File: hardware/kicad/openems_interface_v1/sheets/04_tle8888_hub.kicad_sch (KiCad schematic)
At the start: 5 parts, among them U3 TLE8888-2QK

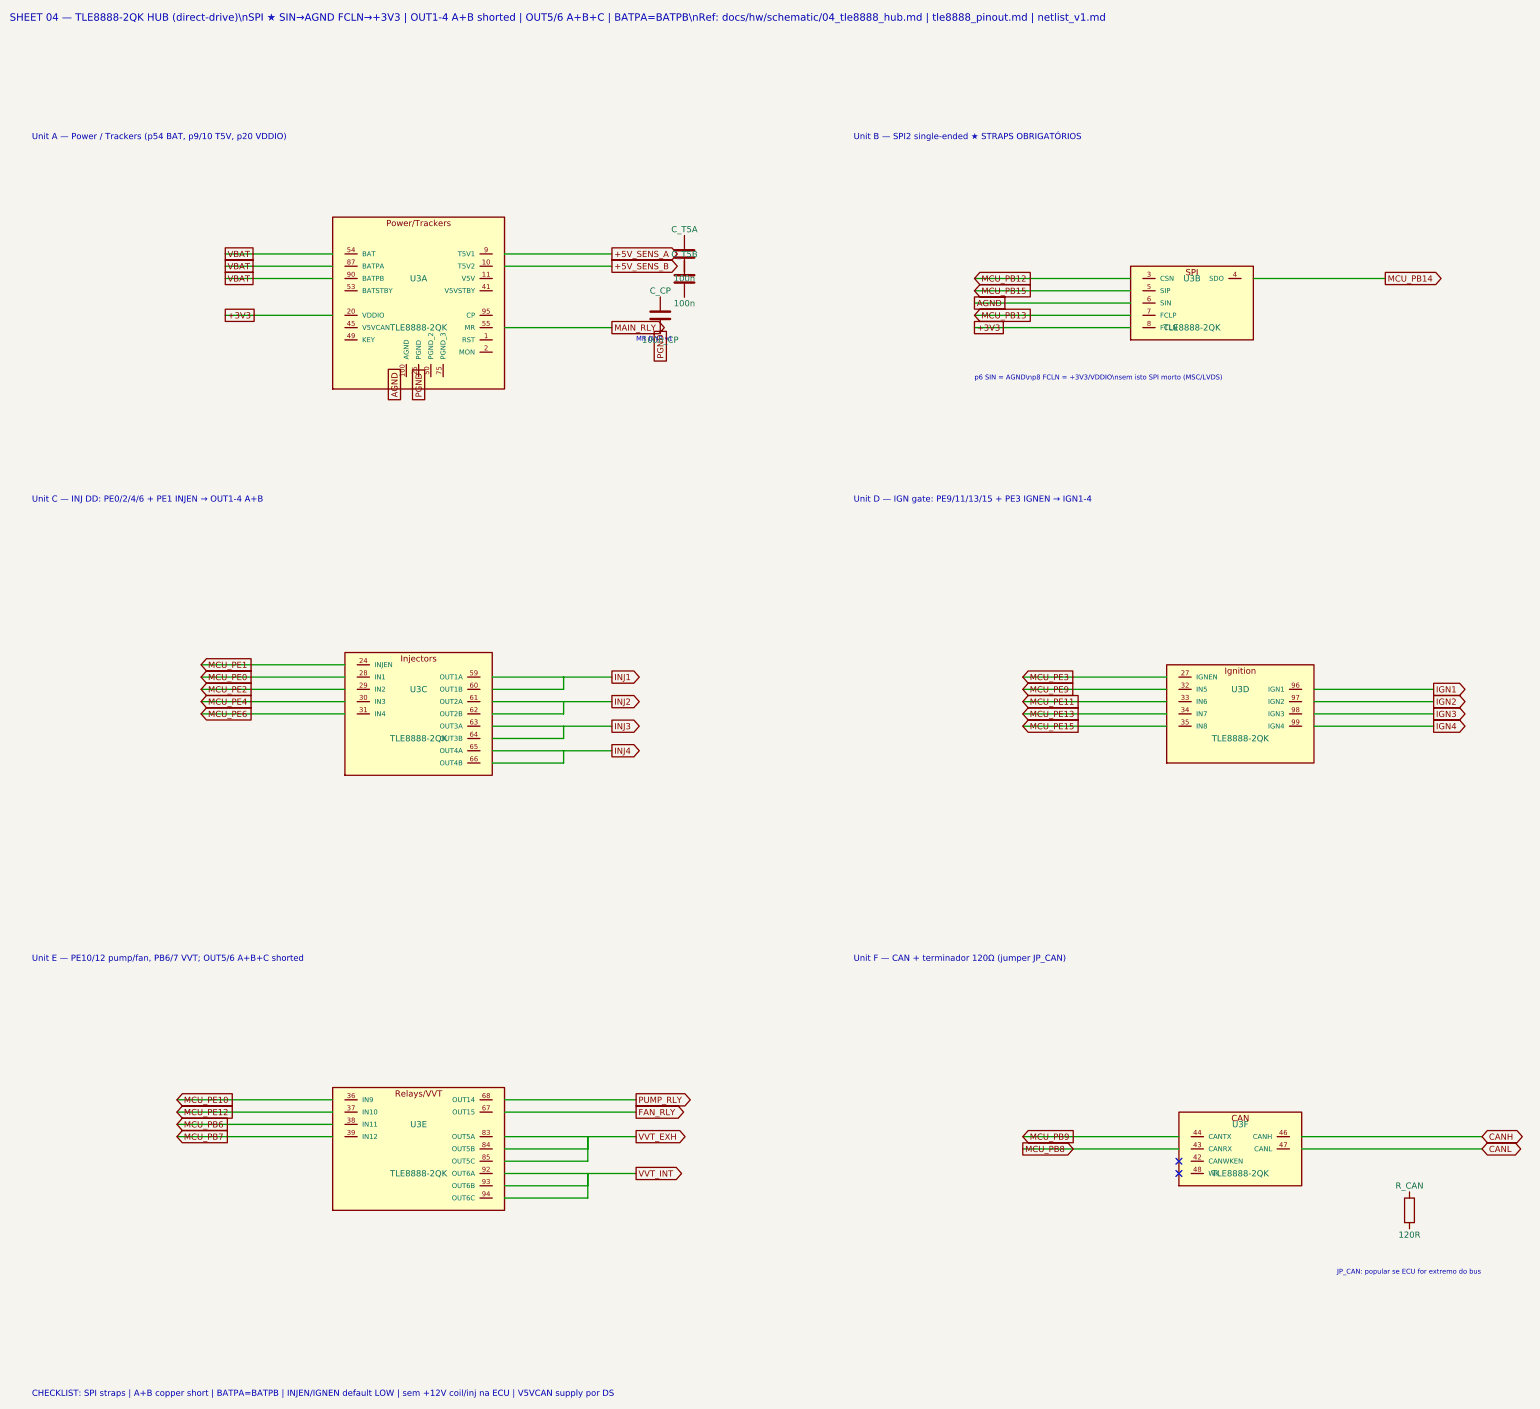
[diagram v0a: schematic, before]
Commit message: feat(hw): nets J1/J2 no PCB + zones PGND + star GND no sch
Atribui pads AMPSEAL a partir de pinmap_logical.md (autoridade),
adiciona pours PGND F/B, e evita curto de terras no esquemático
(star só via NetTie no layout). Script annotate_pcb_nets.py.
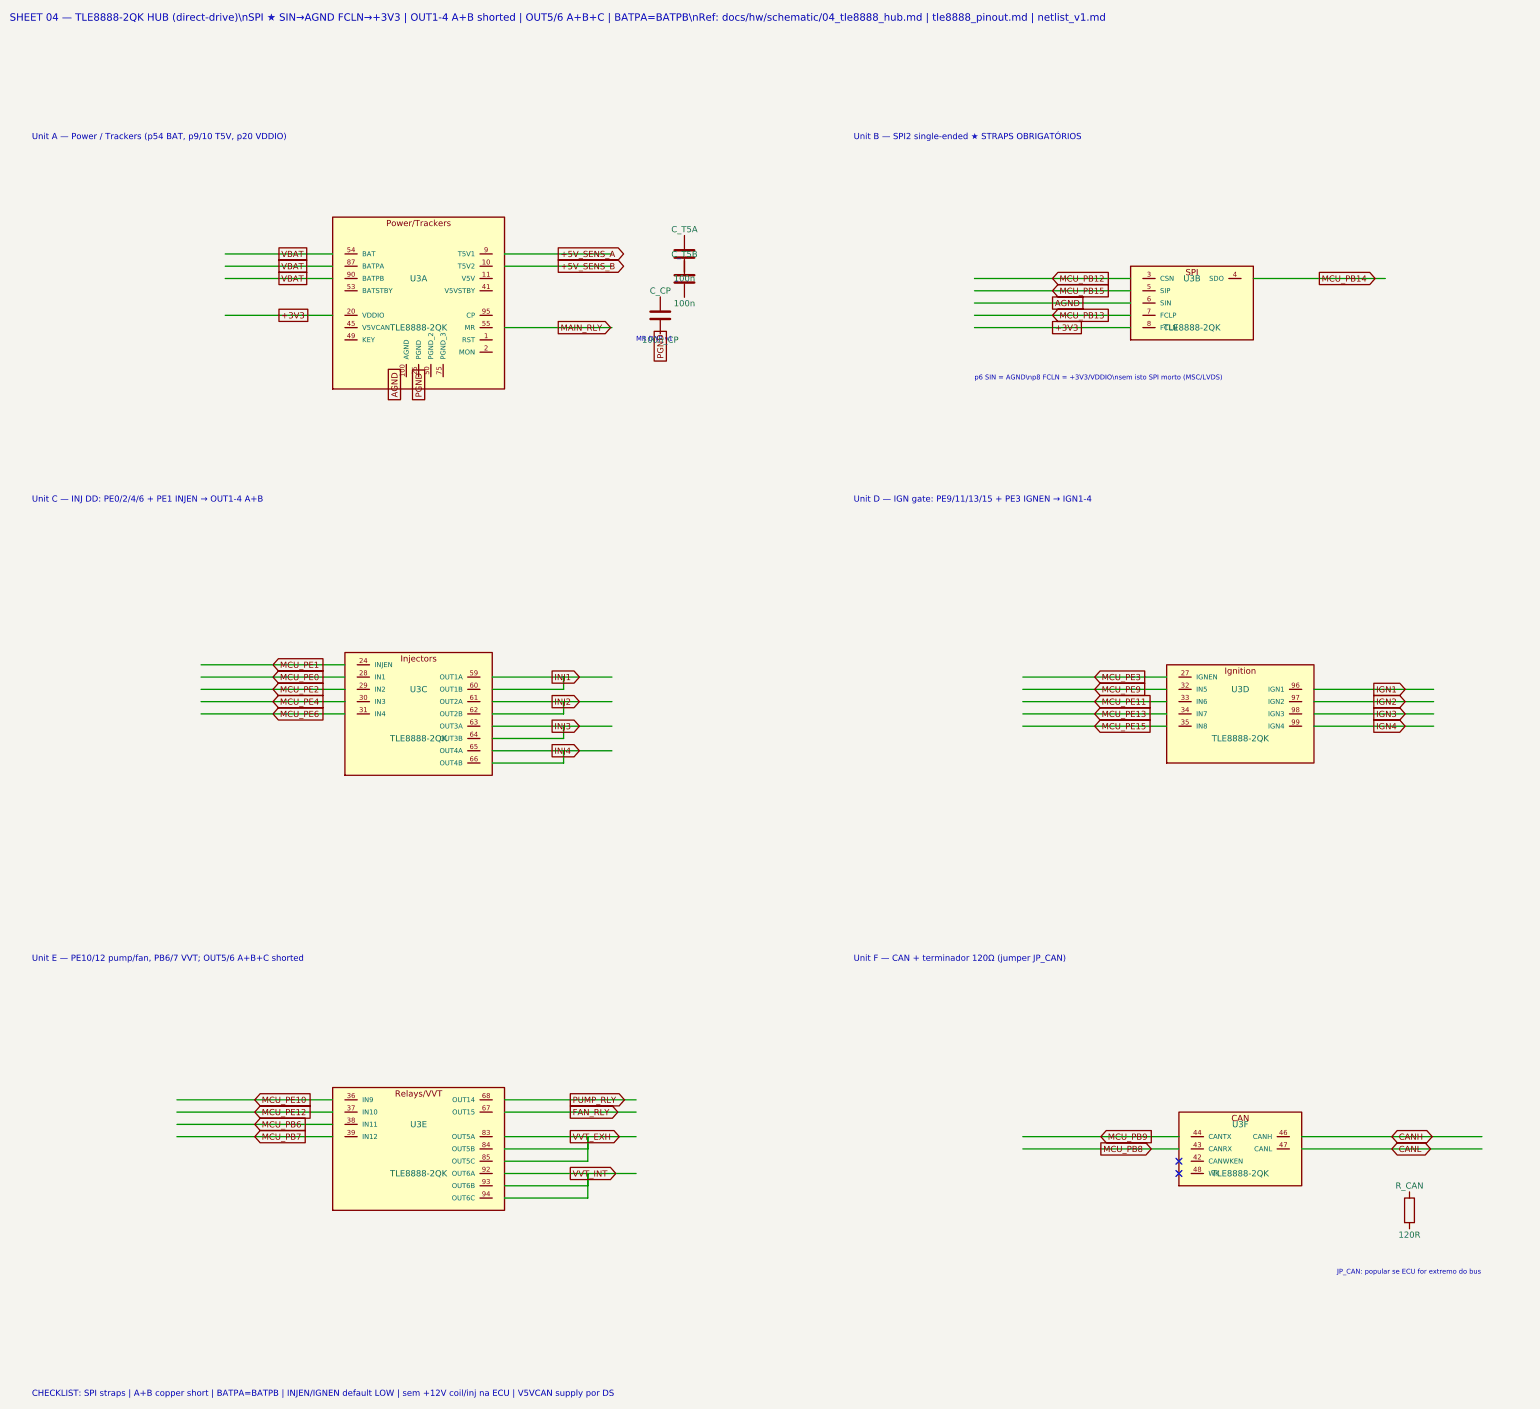
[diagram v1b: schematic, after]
